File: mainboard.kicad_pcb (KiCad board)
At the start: 2 copper layers, 150 x 70 mm, 114 parts, among them J1 HX711, J10 MainPump, J11 WaterLevelSensor, J12 AuxPump, J13 OneWireTemp, J14 OneWireTemp, J15 FlowSensor, J16 USB_C_Receptacle_USB2.0_16P, J17 Conn_01x14_MountingPin, J18 Conn_01x14_MountingPin, J2 Servo, J3 Valve1, J4 Valve2, J5 Valve3, J6 Valve4, J7 Valve5, J8 Valve6, J9 Valve7, Q1 IRLML2502, Q10 DMN3008SFG, Q11 IRLML2502, Q2 IRLML2502, Q3 IRLML2502, Q4 IRLML2502, Q5 IRLML2502, Q6 IRLML2502, Q7 IRLML2502, Q8 IRLML2502, Q9 DMN3008SFG, U1 AP62150WU, U2 DRV8870DDAR, U3 AP33771, U4 USBLC6-2SC6, U5 ESP32-S3-WROOM-1, U6 AP62150WU

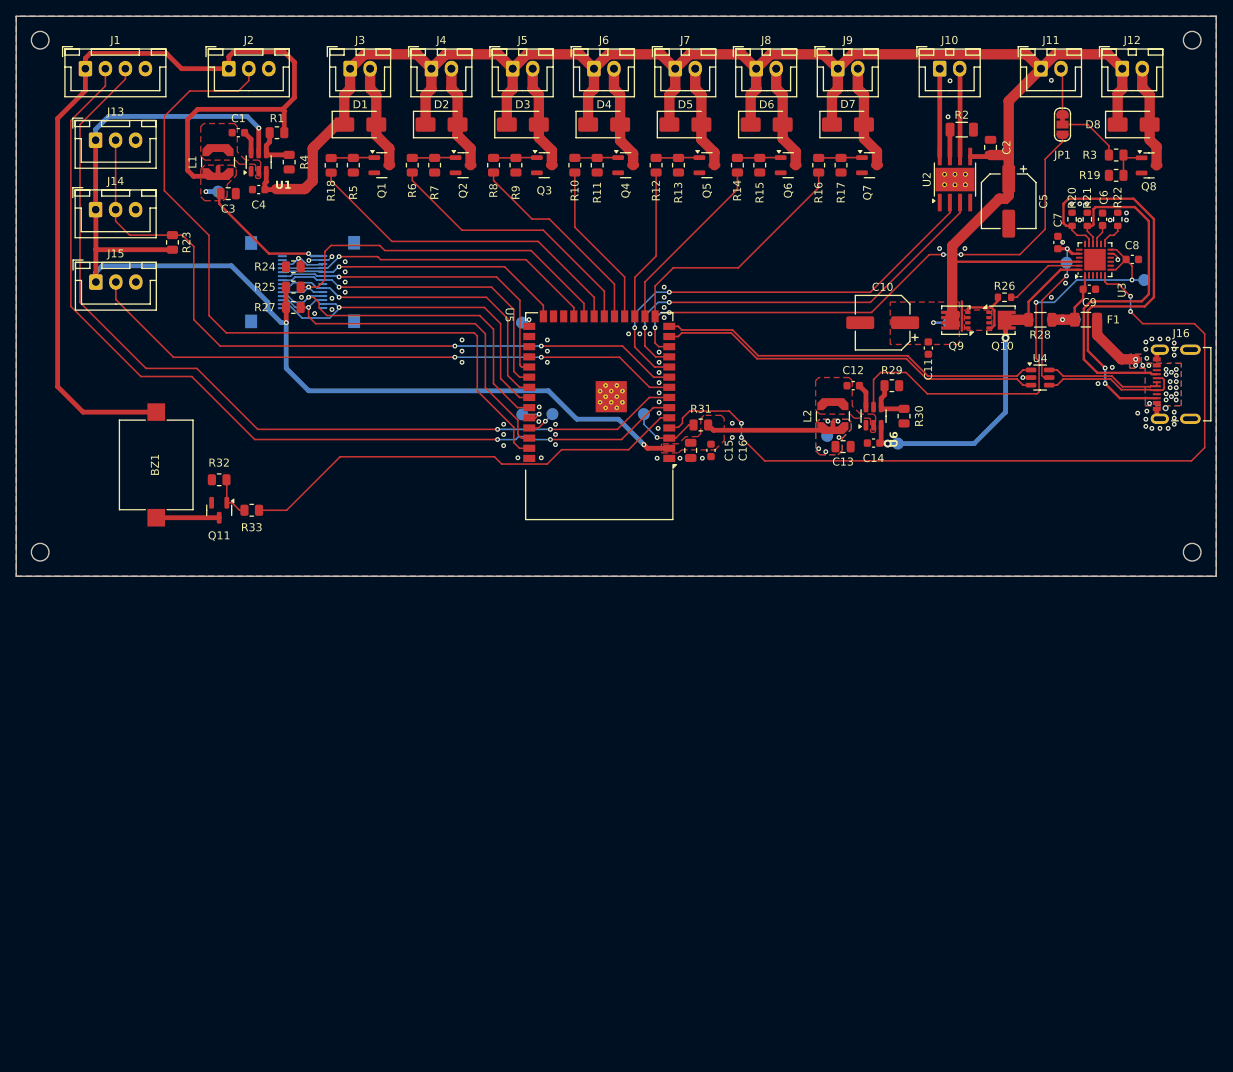
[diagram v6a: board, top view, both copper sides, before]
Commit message: Redesign power rails to use barrel jack 12V input
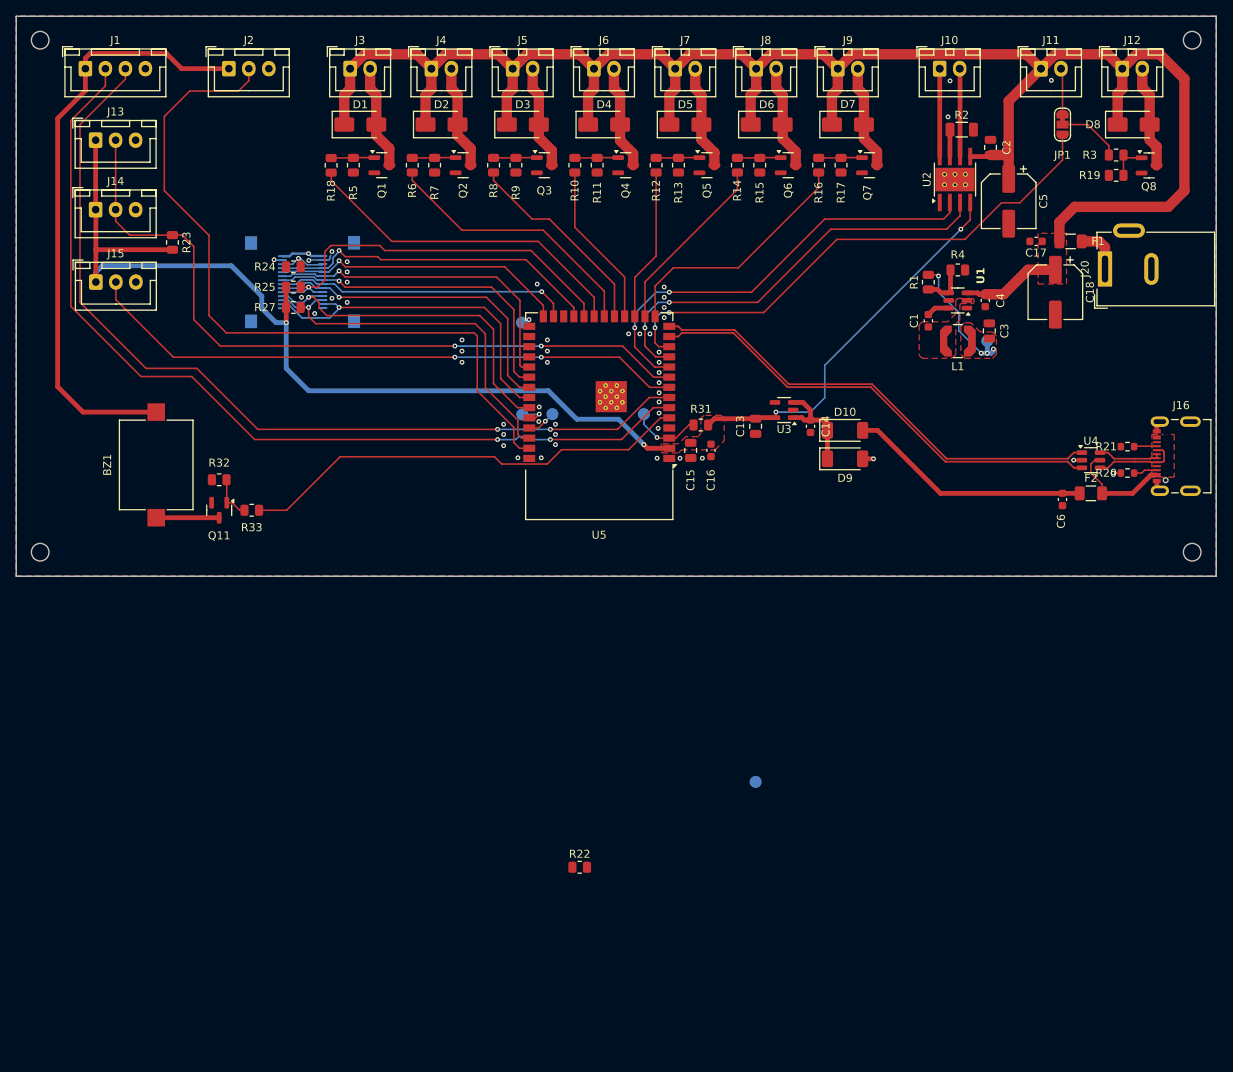
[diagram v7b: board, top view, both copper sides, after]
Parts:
- removed C10: C100u_20V, Capacitor_SMD:CP_Elec_6.3x5.9
- removed C11, C7: C1u_25V, Capacitor_SMD:C_0603_1608Metric
- removed C12, C8: C100n, Capacitor_SMD:C_0603_1608Metric
- removed C9: C10u_25V, Capacitor_SMD:C_0603_1608Metric
- removed L2: L3u3, Inductor_SMD:L_Coilcraft_LPS4018
- removed Q10, Q9: DMN3008SFG, Package_SON:Diodes_PowerDI3333-8
- removed R26: R100, Resistor_SMD:R_0603_1608Metric
- removed R28: R10m_1%_0.5W, Resistor_SMD:R_1206_3216Metric
- removed R29: R31k6_1%, Resistor_SMD:R_0805_2012Metric
- removed R30: R10k_1%, Resistor_SMD:R_0805_2012Metric
- removed TP11, TP2, TP3, TP4, TP5: TestPoint_Small, TestPoint:TestPoint_Pad_D1.5mm
- removed U6: AP62150WU, Package_TO_SOT_SMD:TSOT-23-6
- added C17: C10u_25V, Capacitor_SMD:C_0603_1608Metric, F.Cu at (173.5, 57.1)
- added C18: C100u_20V, Capacitor_SMD:CP_Elec_6.3x5.9, F.Cu at (175.9, 63.5)
- added D10: ME01EA03, Diode_SMD:D_SOD-128, F.Cu at (149.6, 80.8)
- added D9: ME01EA03, Diode_SMD:D_SOD-128, F.Cu at (149.6, 84.3)
- added F2: SF-1206F150-2, Fuse:Fuse_1206_3216Metric, F.Cu at (180.3, 88.6)
- added J20: DC 12V IN, Connector_BarrelJack:BarrelJack_Wuerth_6941xx301002, F.Cu at (182.1, 60.6)
- C6: value C100n -> C10u_25V
- F1: value SF-1206HIA450M-2 -> SF-1206F600M-2
- R22: value R64k9_1% -> R100k; footprint Resistor_SMD:R_0603_1608Metric -> Resistor_SMD:R_0805_2012Metric
- U3: value AP33771 -> TLV75533PDBV; footprint Package_DFN_QFN:QFN-24-1EP_4x4mm_P0.5mm_EP2.7x2.7mm -> Package_TO_SOT_SMD:SOT-23-5
- moved R22 105.3 mm to (116.4, 135.4), turned to 0 degrees
- moved TP1 97.9 mm to (167.4, 69.6), turned to 0 degrees
- moved C3 96.7 mm to (167.6, 68.3), turned to 90 degrees
- moved L1 95.1 mm to (163.7, 69.6), turned to 0 degrees
- moved C4 91.9 mm to (167.1, 64.5), turned to -90 degrees
- moved C1 89.4 mm to (160.0, 67.1), turned to 90 degrees
- moved U1 89.1 mm to (163.7, 64.5), turned to 180 degrees
- moved R4 84.7 mm to (163.7, 60.7), turned to 0 degrees
- moved R1 83.5 mm to (160.0, 62.2), turned to -90 degrees
- moved TP10 44.2 mm to (138.4, 124.7)
- moved U3 43.2 mm to (142.0, 78.2), turned to 180 degrees
- moved C6 35.4 mm to (176.8, 89.4), turned to -90 degrees
- moved R20 32.5 mm to (184.9, 86.1), turned to 180 degrees
- moved R21 28.9 mm to (184.9, 82.8), turned to 180 degrees
- moved U4 12.1 mm to (180.3, 84.5)
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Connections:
- C14 pad 1: /Power/PWR_VCC -> /Power/MCU_LDO_PWR
- C2 pad 1: +15V -> +12V
- C4 pad 1: +15V -> +12V
- C5 pad 1: +15V -> +12V
- C6 pad 1: /Power/IFB -> +5VP
- D1 pad 1: +15V -> +12V
- D2 pad 1: +15V -> +12V
- D3 pad 1: +15V -> +12V
- D4 pad 1: +15V -> +12V
- D5 pad 1: +15V -> +12V
- D6 pad 1: +15V -> +12V
- D7 pad 1: +15V -> +12V
- D8 pad 1: +15V -> +12V
- F1 pad 1: /VBUS_IN -> /Power/DC_IN
- F1 pad 2: /Power/VBUS -> +12V
- J11 pad 1: +15V -> +12V
- J12 pad 1: +15V -> +12V
- J16 pad A4: /VBUS_IN -> /Power/VBUS
- J16 pad A9: /VBUS_IN -> /Power/VBUS
- J16 pad B4: /VBUS_IN -> /Power/VBUS
- J16 pad B9: /VBUS_IN -> /Power/VBUS
- J17 pad 8: unconnected-(J17-Pin_8-Pad8) -> /MCU/LCD_BACKLIGHT
- J18 pad 7: unconnected-(J18-Pin_7-Pad7) -> /MCU/LCD_BACKLIGHT
- J3 pad 1: +15V -> +12V
- J4 pad 1: +15V -> +12V
- J5 pad 1: +15V -> +12V
- J6 pad 1: +15V -> +12V
- J7 pad 1: +15V -> +12V
- J8 pad 1: +15V -> +12V
- J9 pad 1: +15V -> +12V
- R22 pad 1: /Power/PSEL -> +3.3V
- R22 pad 2: GND -> Net-(J20-Pad3)
- U1 pad 3: +15V -> +12V
- U1 pad 5: +3.3V -> unconnected-(U1-EN-Pad5)
- U2 pad 5: +15V -> +12V
- U3 pad 1: /Power/VBUS -> /Power/MCU_LDO_PWR
- U3 pad 2: unconnected-(U3-NC-Pad2) -> GND
- U3 pad 3: GND -> /Power/MCU_LDO_PWR
- U3 pad 5: unconnected-(U3-NC-Pad5) -> +3.3V
- U4 pad 5: /Power/V5V -> /Power/VBUS
- U5 pad 25: unconnected-(U5-IO48-Pad25) -> /MCU/LCD_BACKLIGHT
- U5 pad 4: /Power/FAULT -> unconnected-(U5-IO4-Pad4)
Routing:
- net +15V: track 243.7 -> 0.00 mm, vias 1 -> 0
- net +12V: track 0.00 -> 242.7 mm
- net /Power/FAULT: track 103.7 -> 0.00 mm, vias 4 -> 0
- net /Power/V3VD: track 59.5 -> 0.00 mm, vias 2 -> 0
- net /Power/CC1: track 55.9 -> 2.99 mm, vias 2 -> 0
- net /Power/CC2: track 47.3 -> 2.86 mm
- net /Power/PWR_VCC: track 44.3 -> 0.00 mm, vias 2 -> 0
- net +5V: track 137.4 -> 98.4 mm, vias 2 -> 6
- net /MCU/LCD_BACKLIGHT: track 0.00 -> 37.0 mm, vias 0 -> 1
- net +5VP: track 0.00 -> 30.4 mm
- net /Power/V5V: track 21.1 -> 0.00 mm, vias 2 -> 0
- net /Power/MCU_LDO_PWR: track 0.00 -> 12.9 mm
- net /MCU/USB_D-: track 48.1 -> 58.7 mm
- net /MCU/USB_D+: track 48.1 -> 58.7 mm
- net /Power/PWR_EN: track 10.2 -> 0.00 mm
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- added copper zone on F.Cu, net +12V
- added copper zone on In2.Cu, net +5V
- added copper zone on F.Cu, net /Power/VBUS
- added copper zone on In1.Cu, net GND
- removed copper zone on F.Cu, net +15V
- removed copper zone on B.Cu, net +3.3V
- removed copper zone on F.Cu, net /Power/3V3_BUCK_SW
- removed copper zone on F.Cu, net /Power/PWR_SOURCE_DRAIN
- removed copper zone on B.Cu, net /VBUS_IN
- removed copper zone on F.Cu, net /VBUS_IN
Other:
- copper layers 2 -> 4

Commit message: Cleanup layout and schematic
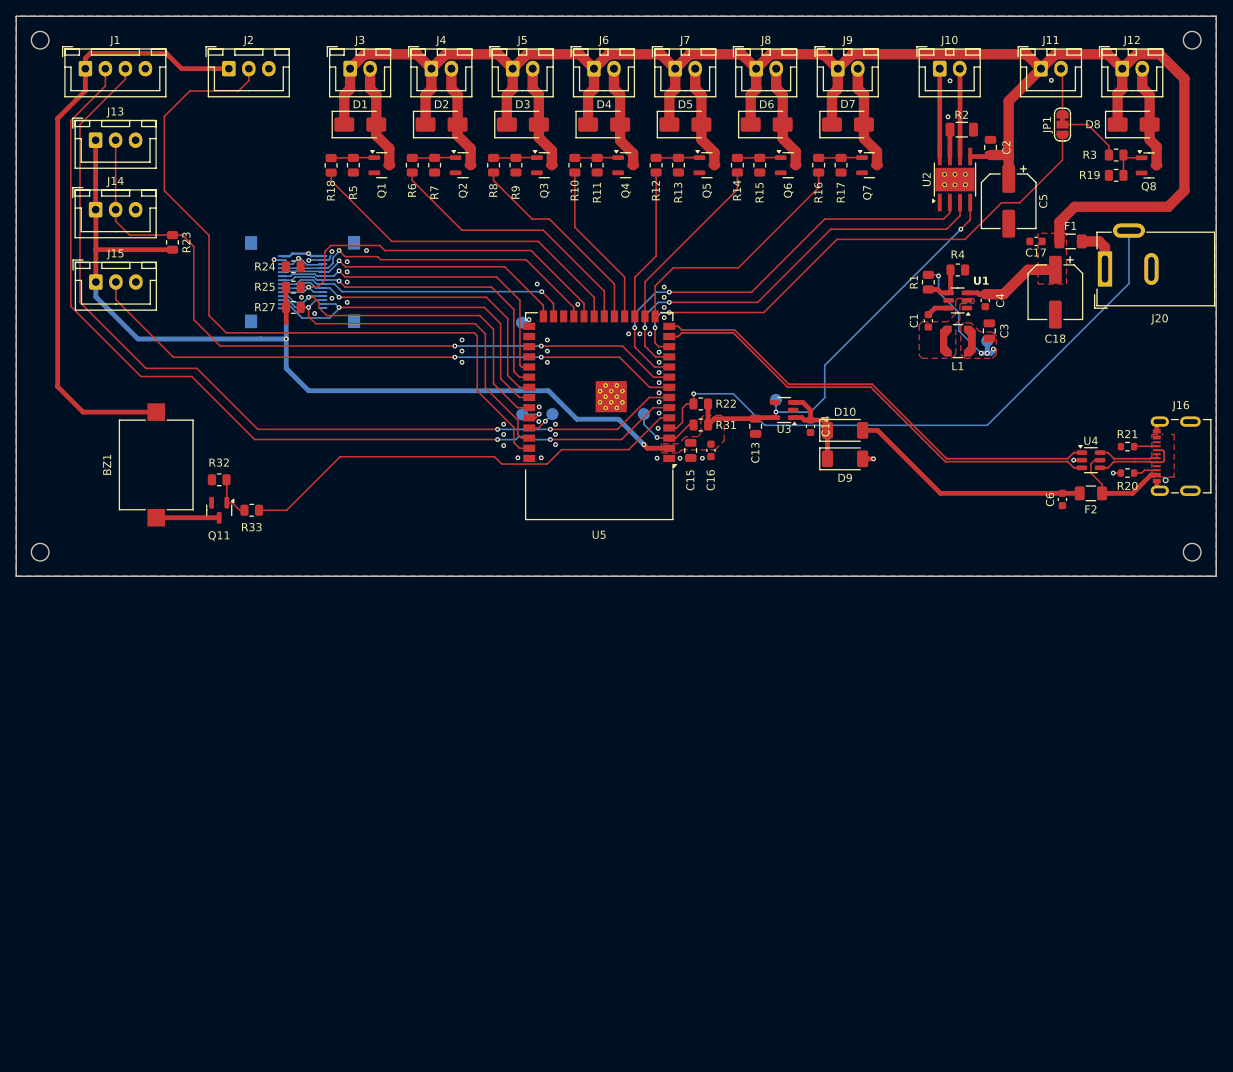
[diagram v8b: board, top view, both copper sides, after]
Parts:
- moved R22 59.9 mm to (131.6, 77.5), turned to 180 degrees
- moved TP10 47.8 mm to (141.0, 77.0)
- moved G*** 10.2 mm to (66.7, 90.0)
- moved G*** 10.2 mm to (66.7, 83.0)
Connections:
- J20 pad 3: Net-(J20-Pad3) -> /MCU/EXT_POWER
- R22 pad 2: Net-(J20-Pad3) -> /MCU/EXT_POWER
- U5 pad 4: unconnected-(U5-IO4-Pad4) -> /MCU/EXT_POWER
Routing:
- net /MCU/EXT_POWER: track 0.00 -> 76.6 mm, vias 0 -> 1
- net +3.3V: track 166.9 -> 169.7 mm
- net GND: vias 50 -> 52
